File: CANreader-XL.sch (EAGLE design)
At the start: 75 parts, among them IC2 TJA1055T, IC3 BD9G101G, IC4 LM1117IMPX-3.3, IC5 STM32F107VBT, Q1 16MHz, SW1 SLEEP, SW2 TERM, U1 HC_05, U2 MCP2551, X1 MINI-USB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

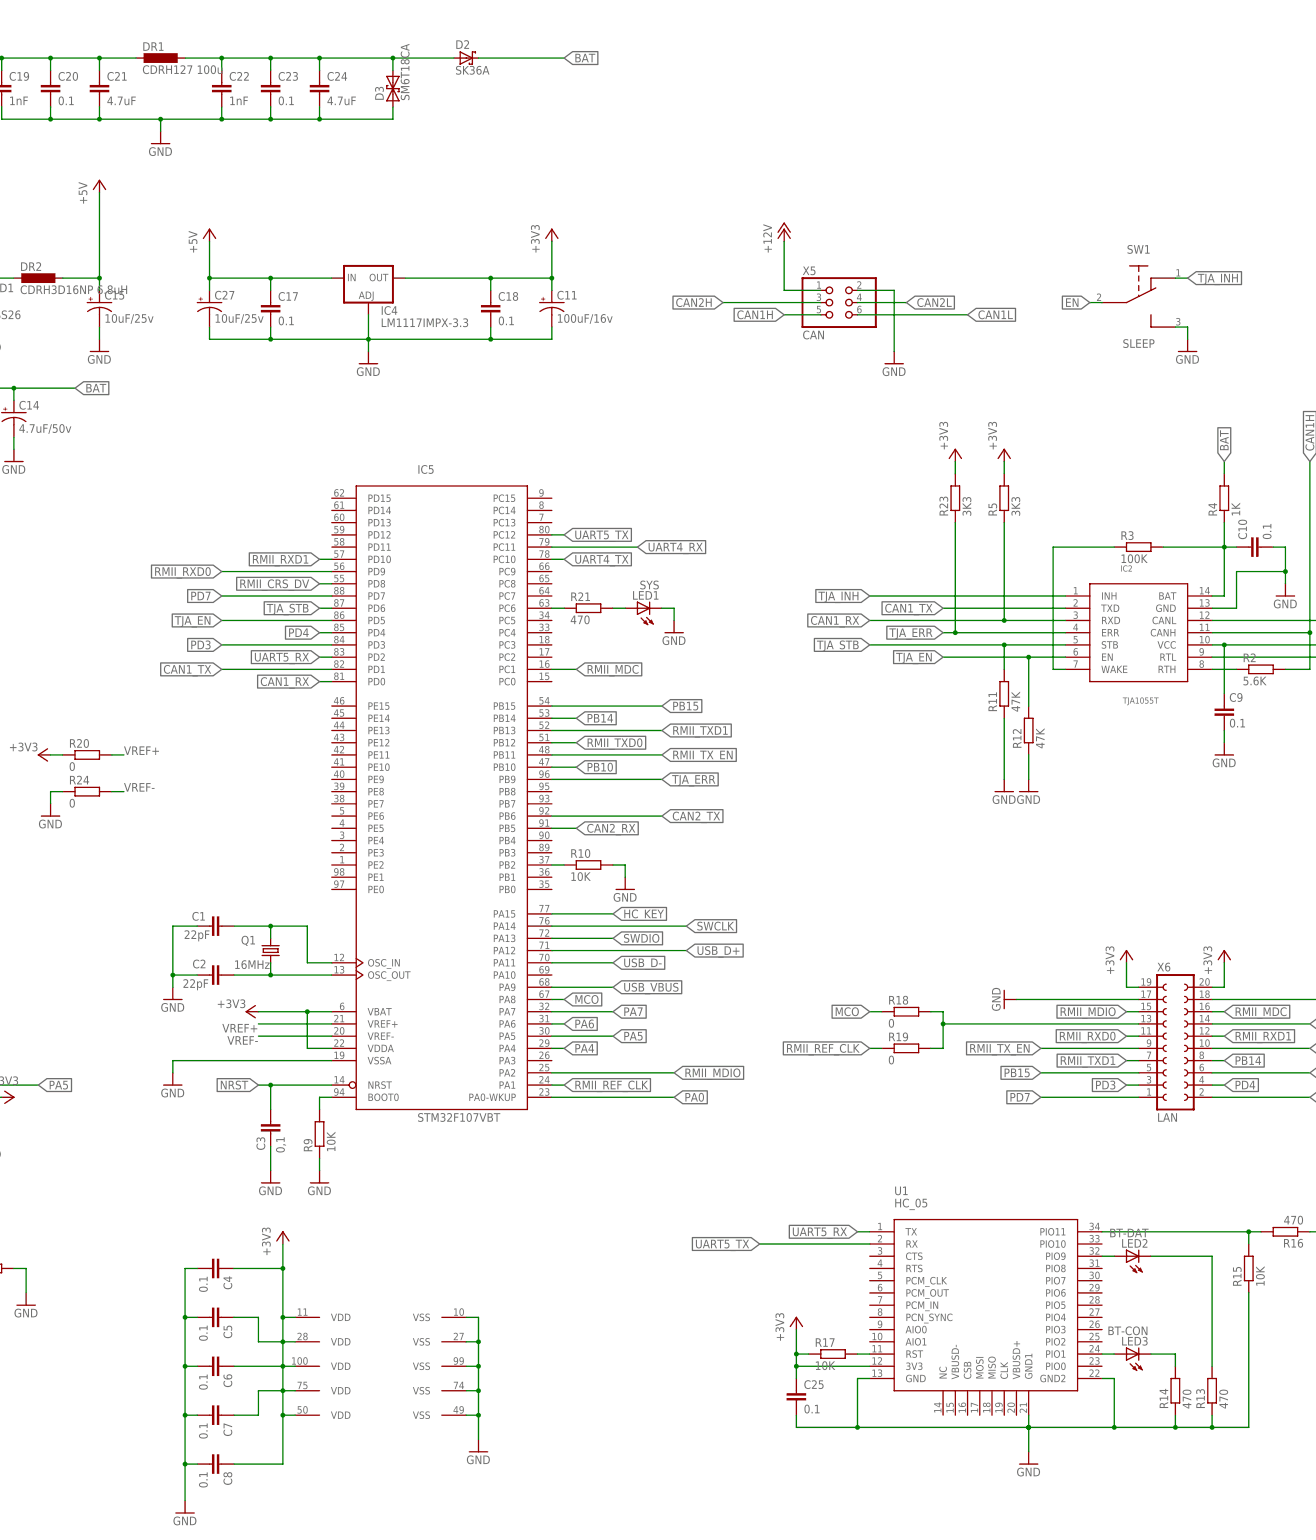
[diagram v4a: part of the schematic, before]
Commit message: Capacitors improvements, HC RST to CPU
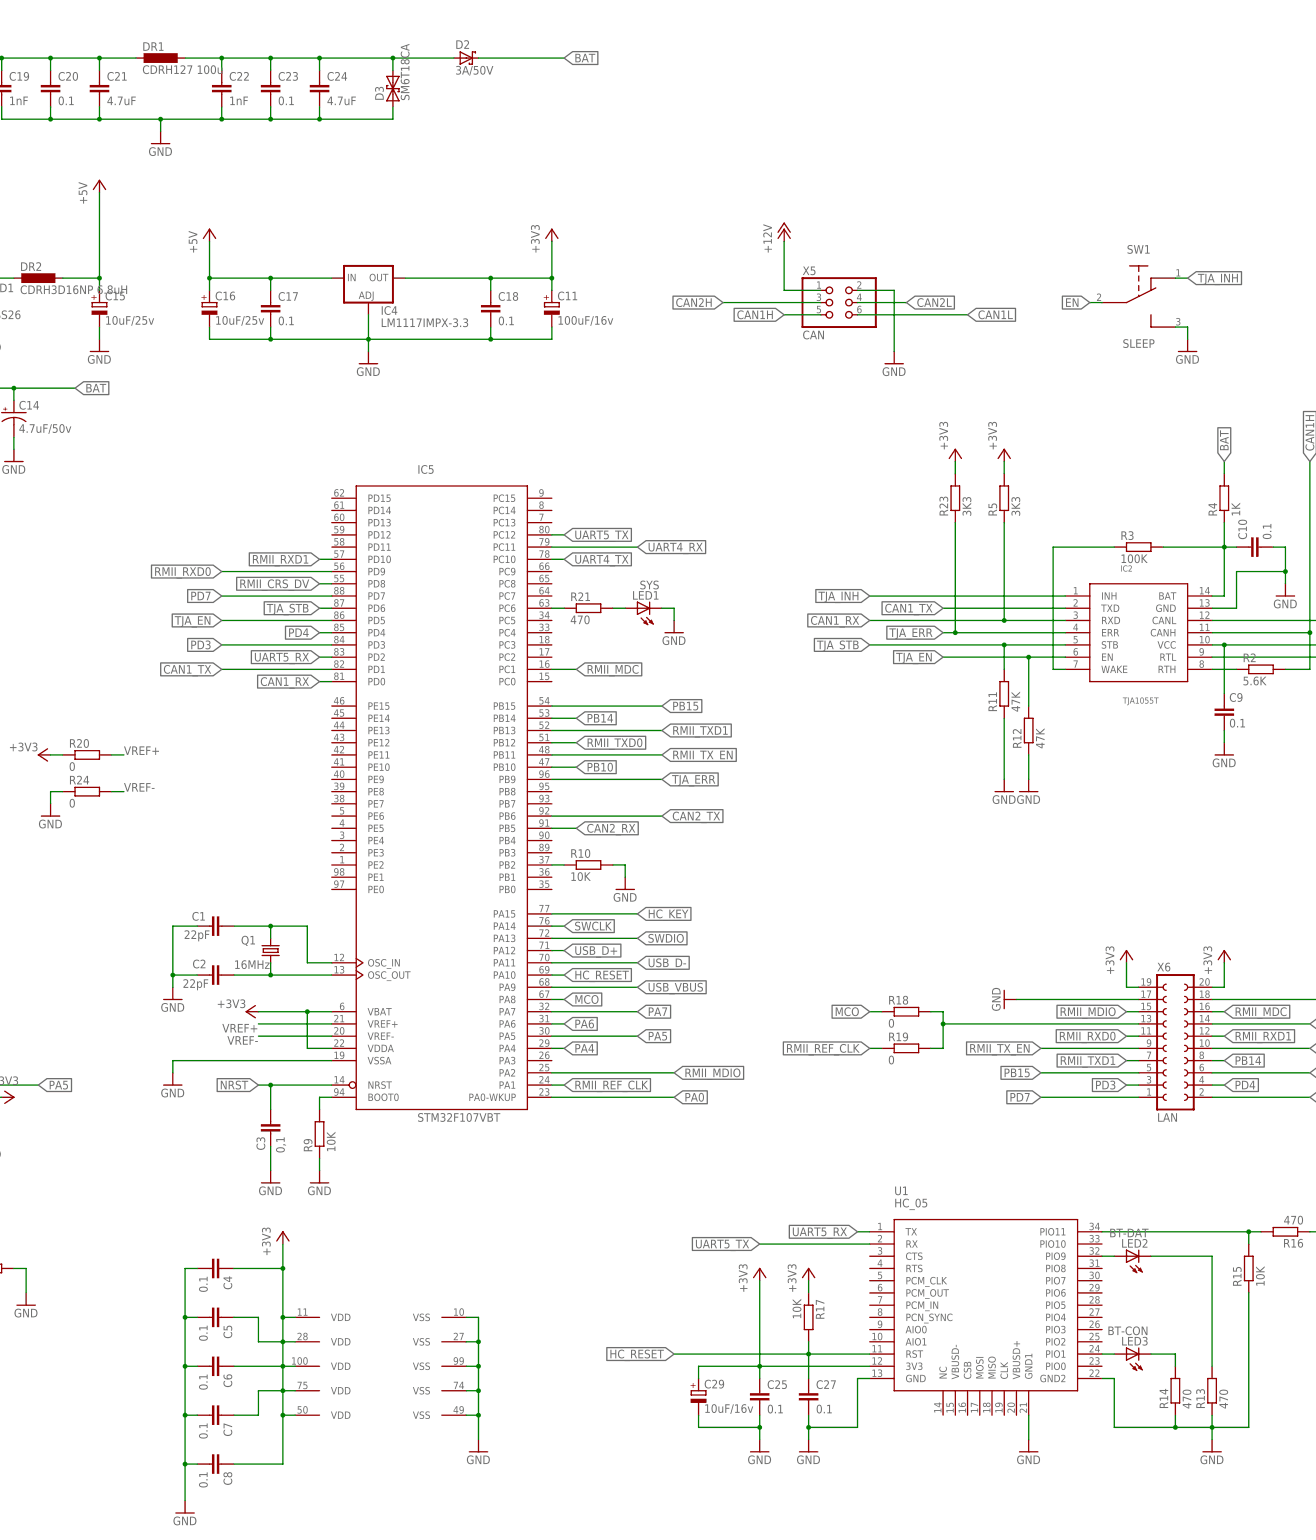
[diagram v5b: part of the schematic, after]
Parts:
- added C16: 10uF/25v, rcl:CPOL-EUSMCC
- added C29: 10uF/16v, rcl:CPOL-EUSMCA
- C11: device rcl:CPOL-US153CLV-0605 -> rcl:CPOL-EUSMCD
- C15: device rcl:CPOL-US153CLV-0505 -> rcl:CPOL-EUSMCC
- C27: value 10uF/25v -> 0.1; device rcl:CPOL-US153CLV-0505 -> rcl:C-EUC0805
- D2: value SK36A -> 3A/50V; device STM32_CAN-USB:SK36A -> diode:SCHOTTKY-DIODESMC
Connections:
- removed net N$24: R17.2, U1.RST
- new net HC_RESET: C27.1, IC5MCU.PA10, R17.2, U1.RST
- net +3V3: now also C29.+
- net +5V: now also C16.+; no longer C27.+
- net GND: now also C16.-, C27.2, C29.-; no longer C27.-
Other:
- moved on the sheet: C25, R17

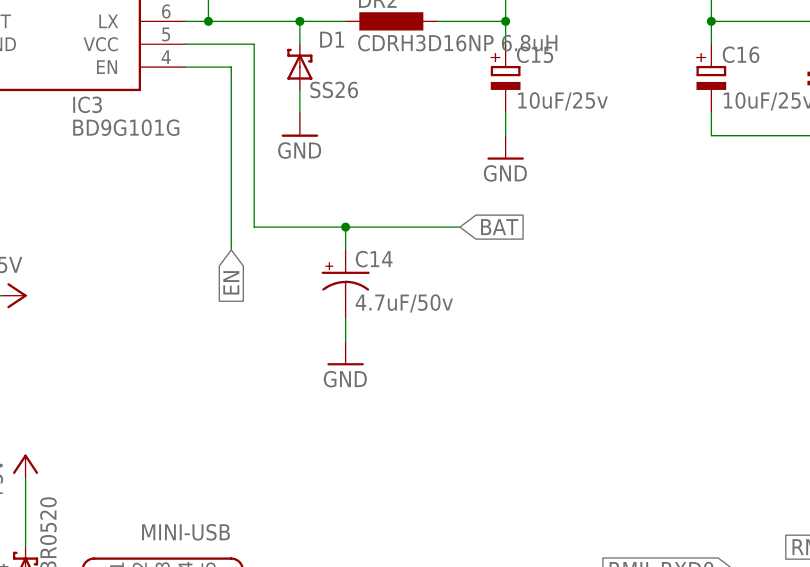
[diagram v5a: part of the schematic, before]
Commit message: Connectors silk
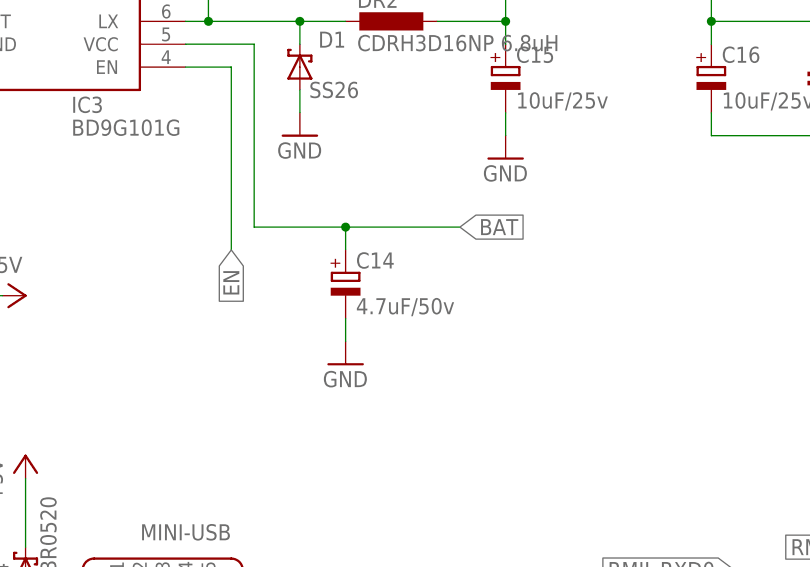
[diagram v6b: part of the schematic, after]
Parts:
- C14: device rcl:CPOL-US153CLV-0505 -> rcl:CPOL-EU153CLV-0505
- X2: device pinhead:PINHD-1X4 -> STM32_CAN-USB:PINHD-1X4
- X3, X5: device pinhead:PINHD-2X3/90 -> STM32_CAN-USB:PINHD-2X3/90
- X4: device pinhead:PINHD-1X4/90 -> STM32_CAN-USB:PINHD-1X4/90
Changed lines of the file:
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@@
 <part name="P+9" library="supply1" deviceset="+12V" device=""/>
 <part name="+3V3" library="supply1" deviceset="+3V3" device=""/>
-<part name="X4" library="pinhead" deviceset="PINHD-1X4" device="/90" value="UART"/>
 <part name="+3V9" library="supply1" deviceset="+3V3" device=""/>
 <part name="R21" library="rcl" deviceset="R-EU_" device="R0805" value="470"/>
@@
 <part name="R22" library="rcl" deviceset="R-EU_" device="R0805" value="120"/>
 <part name="X6" library="con-lsta" deviceset="FE10-2W" device="" value="LAN"/>
-<part name="X2" library="pinhead" deviceset="PINHD-1X4" device="" value="SWD"/>
-<part name="X3" library="pinhead" deviceset="PINHD-2X3" device="/90" value="GPIO"/>
 <part name="LED2" library="led" deviceset="LED" device="3MM" value="BT-DAT"/>
 <part name="LED3" library="led" deviceset="LED" device="3MM" value="BT-CON"/>
 <part name="LED1" library="led" deviceset="LED" device="3MM" value="SYS"/>
-<part name="X5" library="pinhead" deviceset="PINHD-2X3" device="/90" value="CAN"/>
 <part name="SW2" library="STM32_CAN-USB" deviceset="SS12F27" device="" value="TERM"/>
 <part name="SW1" library="STM32_CAN-USB" deviceset="SS12F27" device="" value="SLEEP"/>
@@
 <part name="+3V12" library="supply1" deviceset="+3V3" device=""/>
 <part name="GND25" library="supply1" deviceset="GND" device=""/>
-<part name="C14" library="rcl" deviceset="CPOL-US" device="153CLV-0505" value="4.7uF/50v"/>
 <part name="+3V13" library="supply1" deviceset="+3V3" device=""/>
 <part name="C27" library="rcl" deviceset="C-EU" device="C0805" value="0.1"/>
@@
 <part name="C15" library="rcl" deviceset="CPOL-EU" device="SMCC" value="10uF/25v"/>
 <part name="D2" library="diode" deviceset="SCHOTTKY-DIODE" device="SMC" value="3A/50V"/>
+<part name="C14" library="rcl" deviceset="CPOL-EU" device="153CLV-0505" value="4.7uF/50v"/>
+<part name="X5" library="STM32_CAN-USB" deviceset="PINHD-2X3" device="/90" value="CAN"/>
+<part name="X3" library="STM32_CAN-USB" deviceset="PINHD-2X3" device="/90" value="GPIO"/>
+<part name="X4" library="STM32_CAN-USB" deviceset="PINHD-1X4" device="/90" value="UART"/>
+<part name="X2" library="STM32_CAN-USB" deviceset="PINHD-1X4" device="" value="SWD"/>
 </parts>
 <sheets>
@@
 <instance part="P+9" gate="1" x="154.94" y="147.32"/>
 <instance part="+3V3" gate="G$1" x="-5.08" y="-33.02" rot="R270"/>
-<instance part="X4" gate="A" x="-22.86" y="-5.08"/>
 <instance part="+3V9" gate="G$1" x="-33.02" y="10.16"/>
 <instance part="R21" gate="G$1" x="114.3" y="68.58"/>
@@
 <instance part="R22" gate="G$1" x="-43.18" y="-106.68" rot="R270"/>
 <instance part="X6" gate="1" x="236.22" y="-22.86"/>
-<instance part="X2" gate="A" x="-66.04" y="68.58"/>
-<instance part="X3" gate="A" x="-22.86" y="-30.48"/>
 <instance part="LED2" gate="G$1" x="226.06" y="-66.04" rot="R90"/>
 <instance part="LED3" gate="G$1" x="226.06" y="-86.36" rot="R90"/>
 <instance part="LED1" gate="G$1" x="124.46" y="68.58" rot="R90"/>
-<instance part="X5" gate="A" x="165.1" y="132.08"/>
 <instance part="SW2" gate="G$1" x="-55.88" y="-104.14"/>
 <instance part="SW1" gate="G$1" x="228.6" y="132.08"/>
@@
 </instance>
 <instance part="GND25" gate="1" x="2.54" y="25.4"/>
-<instance part="C14" gate="G$1" x="-5.08" y="109.22"/>
 <instance part="+3V13" gate="G$1" x="149.86" y="-68.58"/>
 <instance part="C27" gate="G$1" x="160.02" y="-93.98"/>
@@
 <instance part="C15" gate="G$1" x="12.7" y="132.08"/>
 <instance part="D2" gate="G$1" x="88.9" y="182.88"/>
+<instance part="C14" gate="G$1" x="-5.08" y="109.22"/>
+<instance part="X5" gate="A" x="165.1" y="132.08"/>
+<instance part="X3" gate="A" x="-22.86" y="-30.48"/>
+<instance part="X4" gate="A" x="-22.86" y="-5.08"/>
+<instance part="X2" gate="A" x="-66.04" y="68.58"/>
 </instances>
 <busses>
@@
 <pinref part="GND12" gate="1" pin="GND"/>
 <wire x1="177.8" y1="121.92" x2="177.8" y2="134.62" width="0.1524" layer="91"/>
+<wire x1="177.8" y1="134.62" x2="170.18" y2="134.62" width="0.1524" layer="91"/>
 <pinref part="X5" gate="A" pin="2"/>
-<wire x1="177.8" y1="134.62" x2="170.18" y2="134.62" width="0.1524" layer="91"/>
 </segment>
 <segment>
@@
 </segment>
 <segment>
-<pinref part="X4" gate="A" pin="1"/>
 <pinref part="+3V9" gate="G$1" pin="+3V3"/>
 <wire x1="-25.4" y1="0" x2="-33.02" y2="0" width="0.1524" layer="91"/>
 <wire x1="-33.02" y1="0" x2="-33.02" y2="7.62" width="0.1524" layer="91"/>
+<pinref part="X4" gate="A" pin="1"/>
 </segment>
 <segment>
@@
 </segment>
 <segment>
-<pinref part="X3" gate="A" pin="6"/>
 <pinref part="+3V3" gate="G$1" pin="+3V3"/>
 <wire x1="-17.78" y1="-33.02" x2="-7.62" y2="-33.02" width="0.1524" layer="91"/>
+<pinref part="X3" gate="A" pin="6"/>
 </segment>
 <segment>
@@
 <pinref part="P+9" gate="1" pin="+12V"/>
 <wire x1="154.94" y1="144.78" x2="154.94" y2="134.62" width="0.1524" layer="91"/>
+<wire x1="154.94" y1="134.62" x2="162.56" y2="134.62" width="0.1524" layer="91"/>
 <pinref part="X5" gate="A" pin="1"/>
-<wire x1="154.94" y1="134.62" x2="162.56" y2="134.62" width="0.1524" layer="91"/>
 </segment>
 </net>
@@
 <segment>
 <label x="-35.56" y="-5.08" size="1.778" layer="95" rot="R180" xref="yes"/>
+<wire x1="-35.56" y1="-5.08" x2="-25.4" y2="-5.08" width="0.1524" layer="91"/>
 <pinref part="X4" gate="A" pin="3"/>
-<wire x1="-35.56" y1="-5.08" x2="-25.4" y2="-5.08" width="0.1524" layer="91"/>
 </segment>
 </net>
@@
 <segment>
 <label x="154.94" y="129.54" size="1.778" layer="95" rot="R180" xref="yes"/>
+<wire x1="154.94" y1="129.54" x2="162.56" y2="129.54" width="0.1524" layer="91"/>
 <pinref part="X5" gate="A" pin="5"/>
-<wire x1="154.94" y1="129.54" x2="162.56" y2="129.54" width="0.1524" layer="91"/>
 </segment>
 </net>
@@
 <segment>
 <label x="180.34" y="132.08" size="1.778" layer="95" xref="yes"/>
+<wire x1="180.34" y1="132.08" x2="170.18" y2="132.08" width="0.1524" layer="91"/>
 <pinref part="X5" gate="A" pin="4"/>
-<wire x1="180.34" y1="132.08" x2="170.18" y2="132.08" width="0.1524" layer="91"/>
 </segment>
 <segment>
@@
 <segment>
 <label x="142.24" y="132.08" size="1.778" layer="95" rot="R180" xref="yes"/>
+<wire x1="142.24" y1="132.08" x2="162.56" y2="132.08" width="0.1524" layer="91"/>
 <pinref part="X5" gate="A" pin="3"/>
-<wire x1="142.24" y1="132.08" x2="162.56" y2="132.08" width="0.1524" layer="91"/>
-</segment>
-<segment>
+</segment>
+<segment>
